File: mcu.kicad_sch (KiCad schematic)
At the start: 1 part, among them U1 STM32F405RGTx

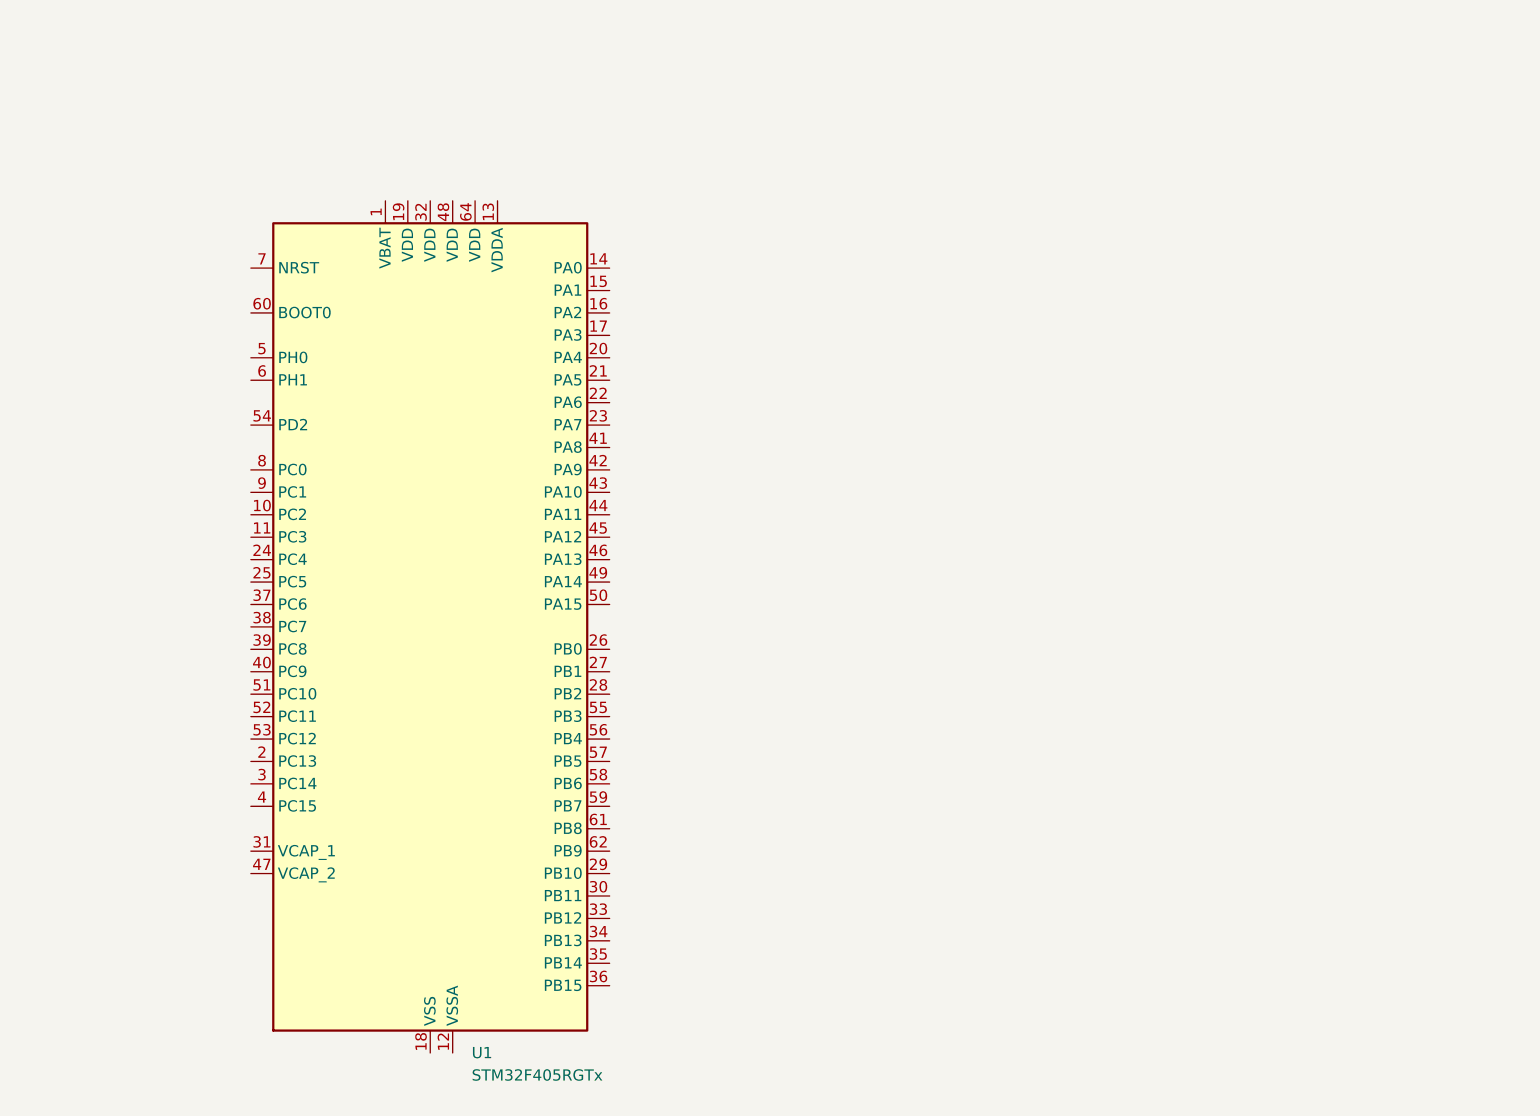
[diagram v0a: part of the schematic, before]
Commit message: Added oled
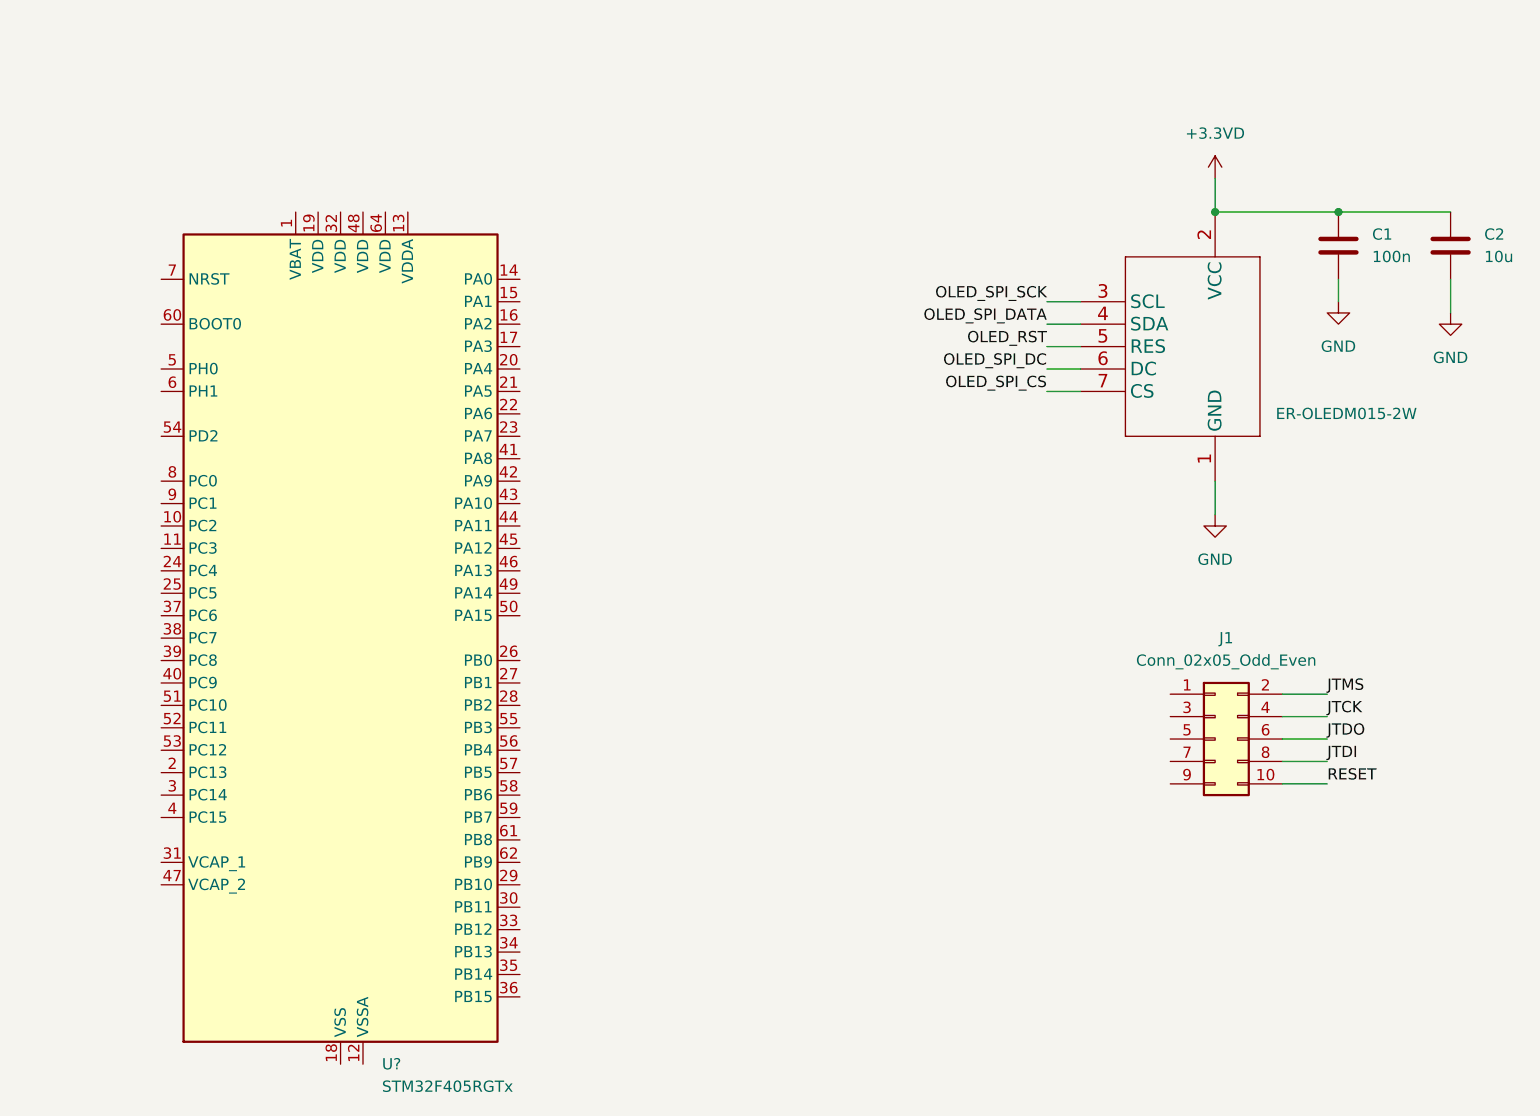
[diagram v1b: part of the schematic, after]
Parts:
- added C1: 100n, symbol Device:C
- added C2: 10u, symbol Device:C
- added ER-OLEDM015-2W: ~, Galerna:ER-OLEDM015-2, symbol Galerna:ER-OLEDM015-SPI
- added J1: Conn_02x05_Odd_Even, symbol Connector_Generic:Conn_02x05_Odd_Even
- renumbered U1 to U?
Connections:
- new net +3.3VD: C1.1, C2.1, ER-OLEDM015-2W.2 (VCC)
- new net GND: C1.2, C2.2, ER-OLEDM015-2W.1 (GND)
- new net JTCK: J1.4 (Pin_4)
- new net JTDI: J1.8 (Pin_8)
- new net JTDO: J1.6 (Pin_6)
- new net JTMS: J1.2 (Pin_2)
- new net OLED_RST: ER-OLEDM015-2W.5 (RES)
- new net OLED_SPI_CS: ER-OLEDM015-2W.7 (CS)
- new net OLED_SPI_DATA: ER-OLEDM015-2W.4 (SDA)
- new net OLED_SPI_DC: ER-OLEDM015-2W.6 (DC)
- new net OLED_SPI_SCK: ER-OLEDM015-2W.3 (SCL)
- new net RESET: J1.10 (Pin_10)
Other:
- moved on the sheet: U?

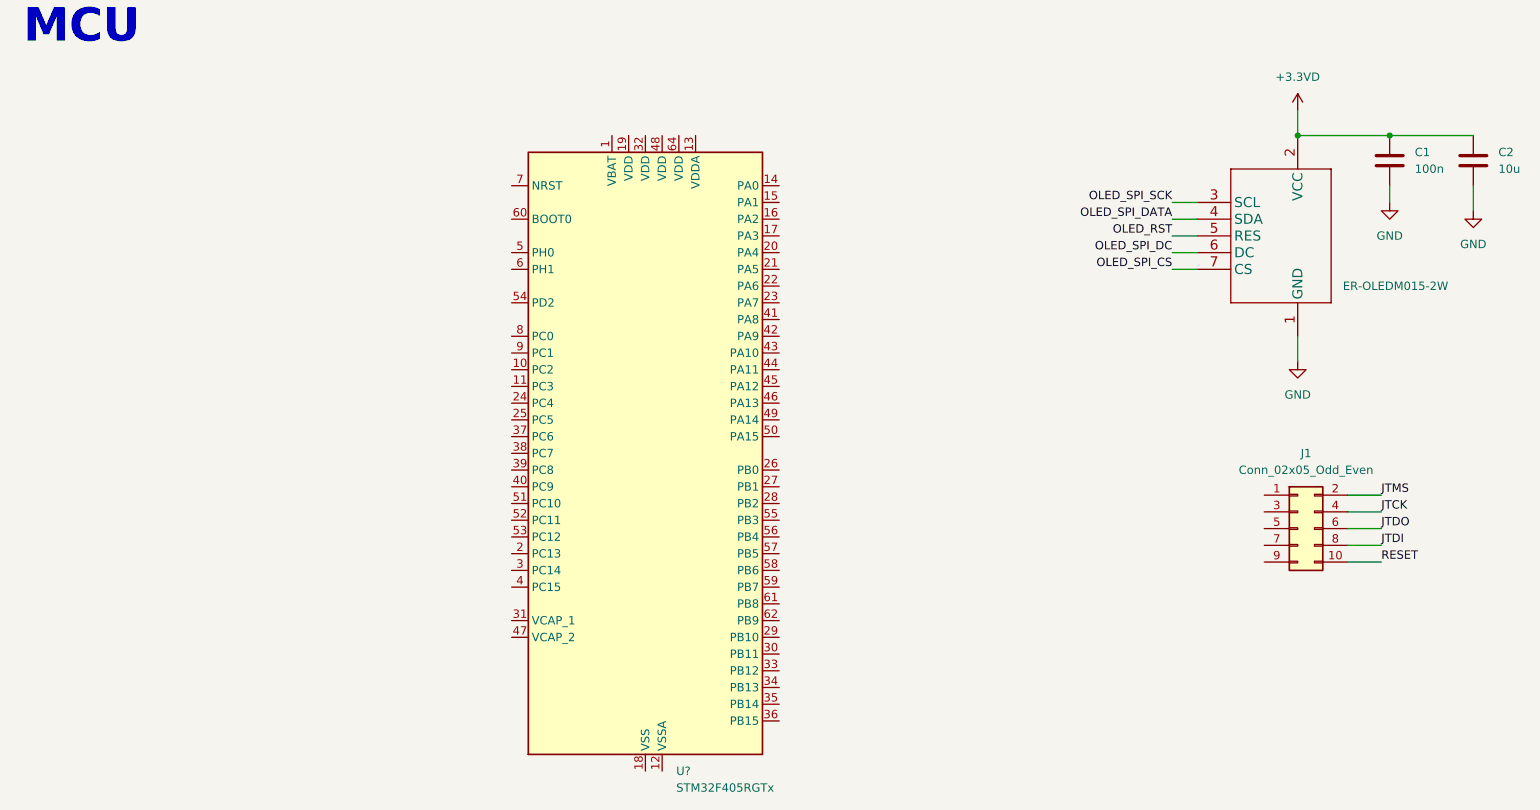
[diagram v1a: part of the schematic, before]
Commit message: SWD connector added
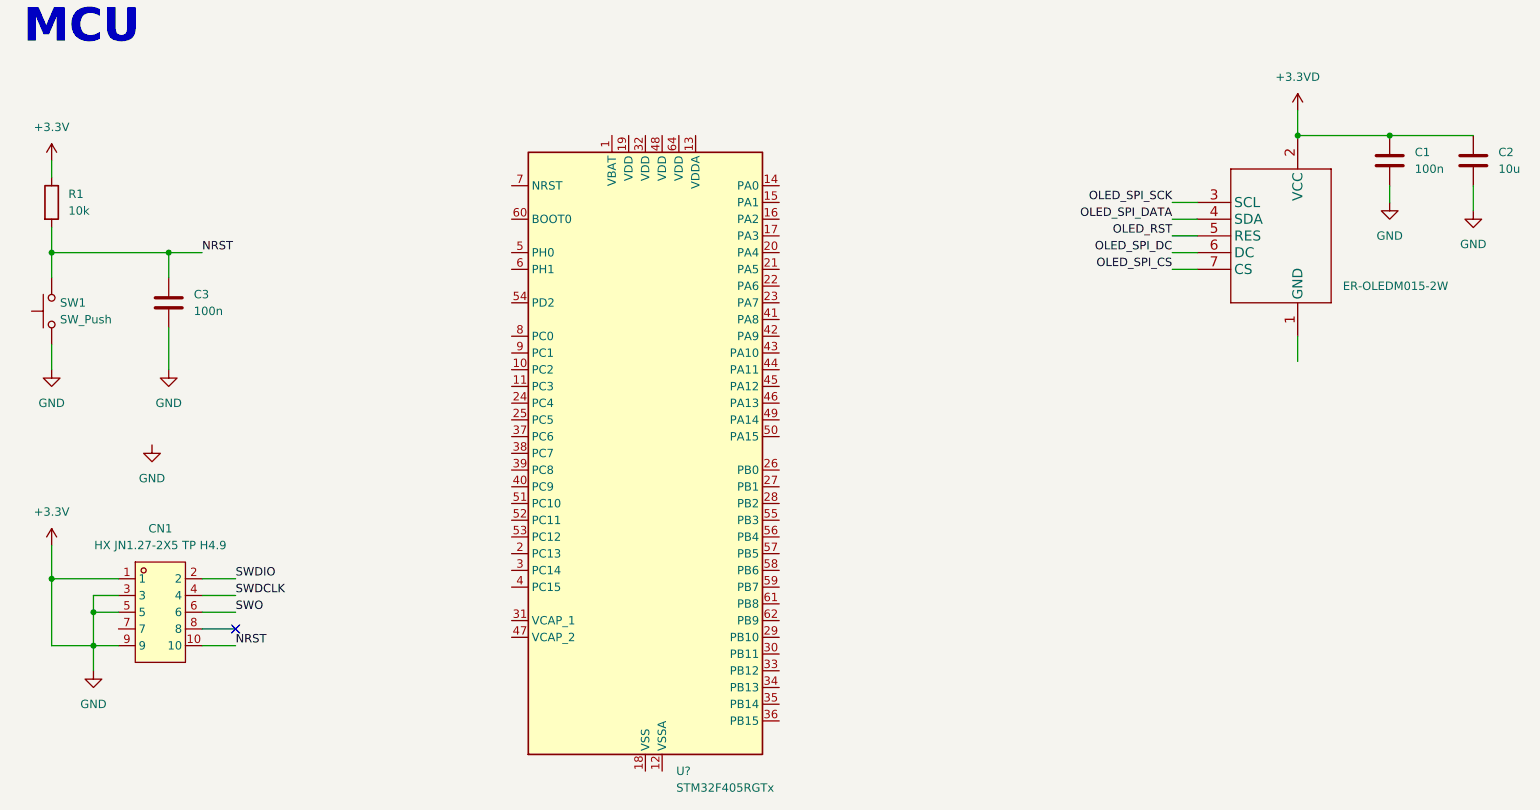
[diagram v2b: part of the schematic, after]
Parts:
- removed J1: Conn_02x05_Odd_Even, symbol Connector_Generic:Conn_02x05_Odd_Even
- added C3: 100n, symbol Device:C
- added CN1: HX JN1.27-2X5 TP H4.9, Galerna:IDC-SMD_10P-P1.27-3220-10-0300-00, symbol Galerna:HXJN1.27-2X5TPH4.9
- added R1: 10k, symbol Device:R
- added SW1: SW_Push, symbol Switch:SW_Push
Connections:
- net GND renamed +3.3V
- net +3.3V: now also C3.2, CN1.1, CN1.3, CN1.5, CN1.9, R1.1, SW1.1; no longer ER-OLEDM015-2W.1 (GND)
- new net NRST: C3.1, CN1.10, R1.2, SW1.2
- new net SWDCLK: CN1.4
- new net SWDIO: CN1.2
- new net SWO: CN1.6
- no-connect marks 0 -> 1

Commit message: extending library
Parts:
- removed SW1: SW_Push, symbol Switch:SW_Push
- added SW1: TS-1088-AR02016, Galerna:SW-SMD_L3.9-W3.0-P4.45, symbol Galerna:TS-1088-AR02016
- gave numbers to parts that had none: 1
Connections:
- net +3.3V: now also SW1.2
- net NRST: now also SW1.1
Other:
- moved on the sheet: C3, CN1, R1

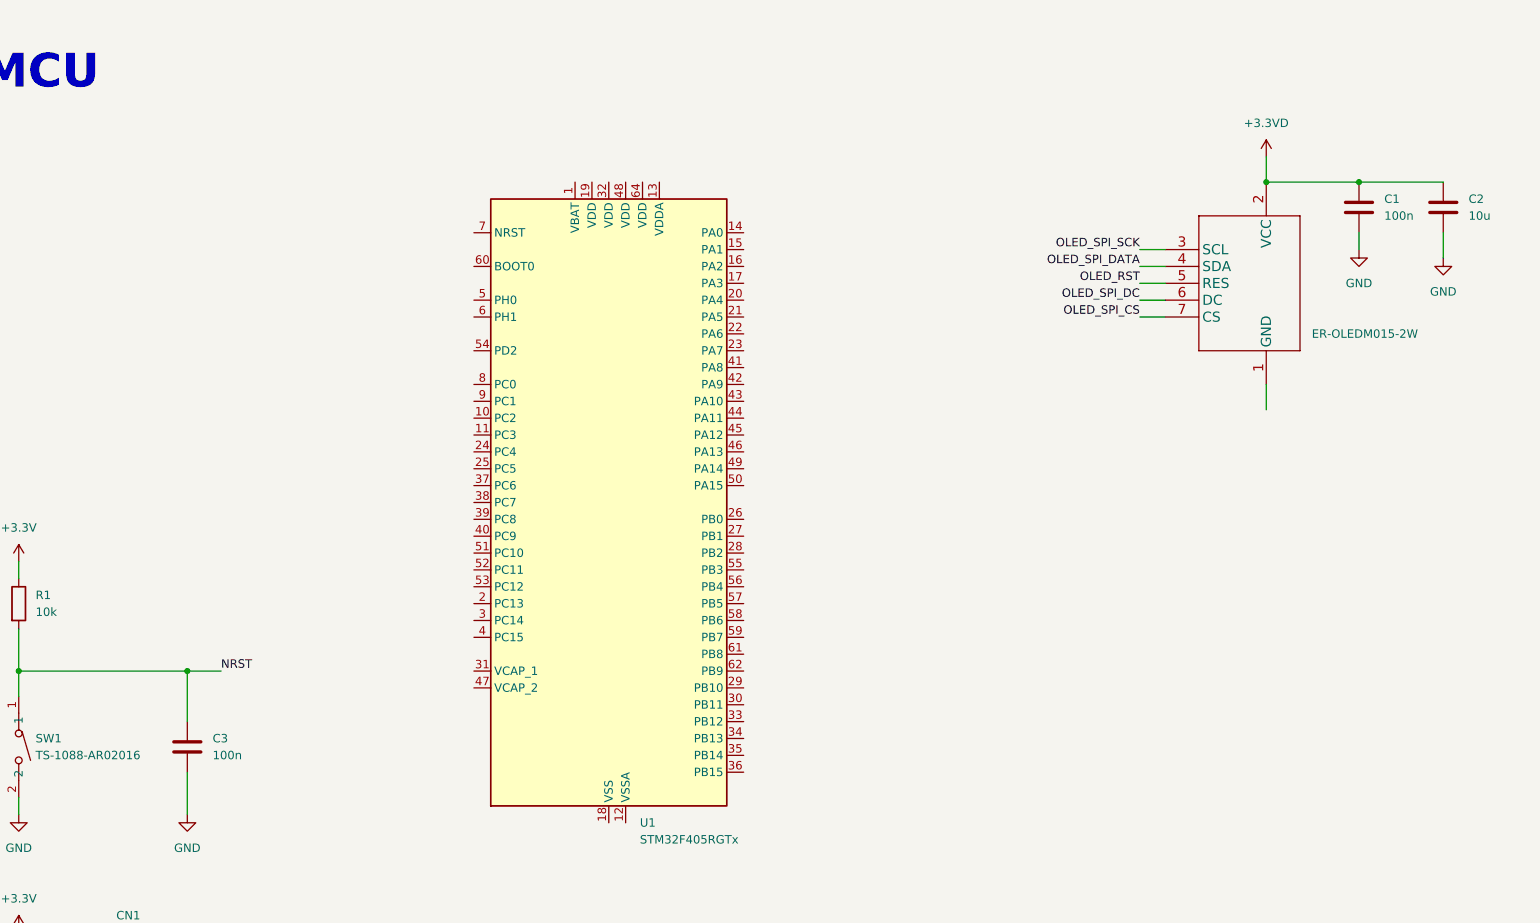
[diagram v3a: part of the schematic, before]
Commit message: adde boot switch
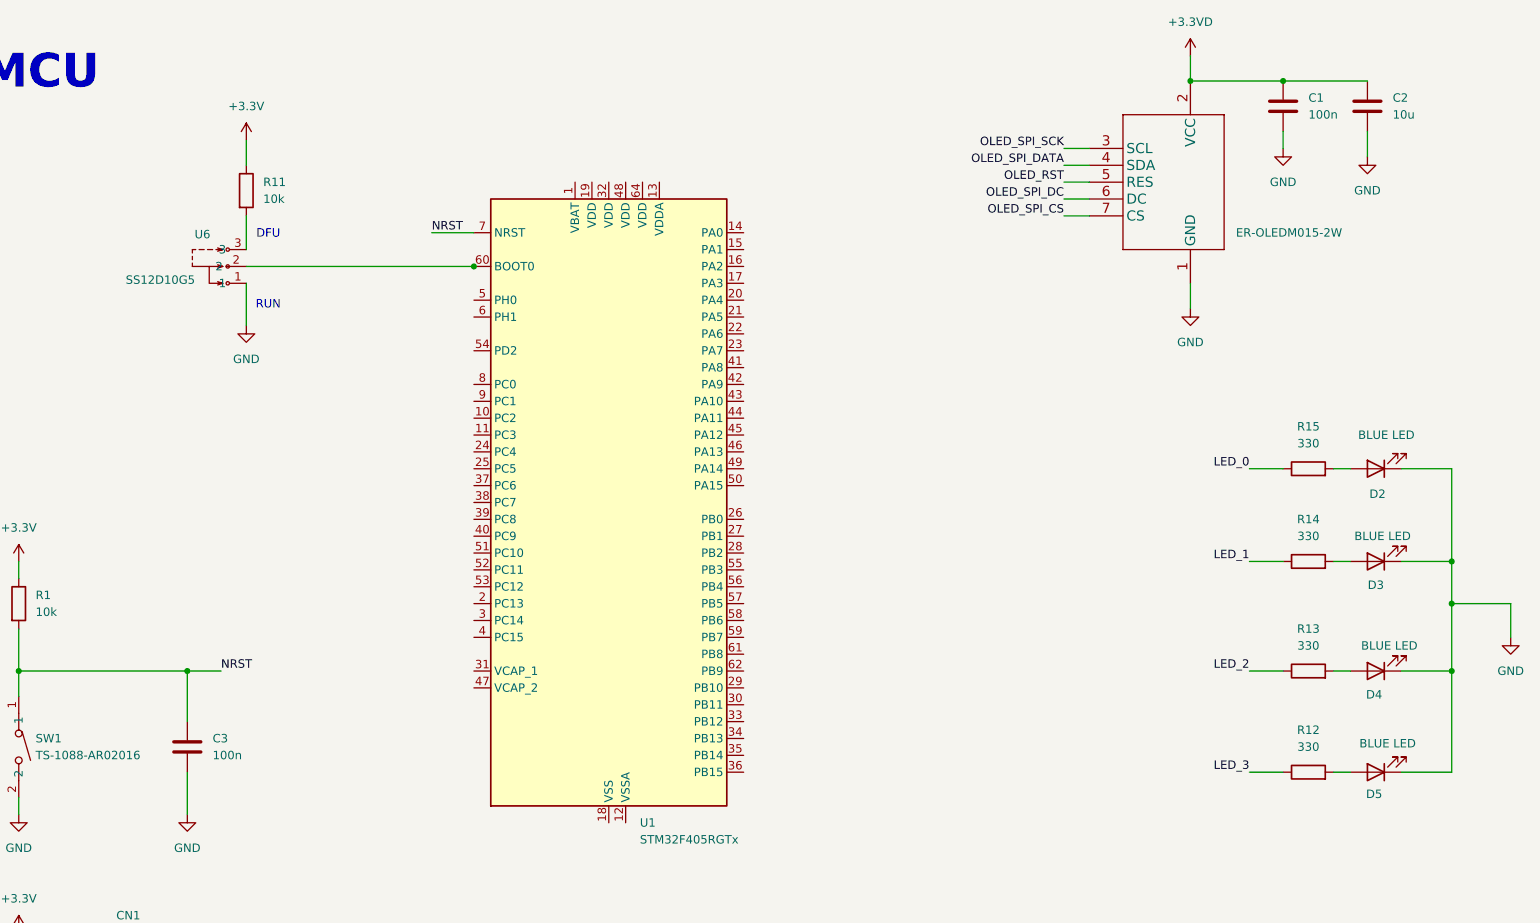
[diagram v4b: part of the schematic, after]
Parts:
- added D2, D3, D4, D5: BLUE LED, symbol Device:LED
- added R11: 10k, symbol Device:R
- added R12, R13, R14, R15: 330, symbol Device:R
- added U6: SS12D10G5, Galerna:SW-TH_SHOU-HAN_SS12D10G4, symbol Galerna:SS12D10G5
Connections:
- net +3.3V: now also ER-OLEDM015-2W.1 (GND), D2.1 (K), D3.1 (K), D4.1 (K), D5.1 (K), R11.1, U6.1
- net NRST: now also U1.7 (NRST)
- net at U1.60 (BOOT0): now also U6.2
- new net: D5.2 (A), R12.2
- new net: D3.2 (A), R14.2
- new net: R11.2, U6.3
- new net: D2.2 (A), R15.2
- new net: D4.2 (A), R13.2
- new net LED_0: R15.1
- new net LED_1: R14.1
- new net LED_2: R13.1
- new net LED_3: R12.1
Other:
- note added: "DFU"
- note added: "RUN"
- moved on the sheet: C1, C2, ER-OLEDM015-2W

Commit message: First pins assingments
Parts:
- removed R11: 10k, symbol Device:R
- added C4: 100n, symbol Device:C
- added C5, C6: 10u, symbol Device:C
- added C7, C8: 12p, symbol Device:C
- added D1: RED, symbol Device:LED
- added FB1: 100@100MHz, symbol Device:FerriteBead
- added J1: DM3CS-SF, Galerna:HRS_DM3CS-SF, symbol Galerna:DM3CS-SF
- added R10: 47k, symbol Device:R
- added R2, R3, R4, R5, R6: 10k, symbol Device:R
- added R7: 22, symbol Device:R
- added R8: 1K, symbol Device:R
- added R9: 10K, symbol Device:R
- added X1: X1E000210127000G, Galerna:CRYSTAL-SMD_4P-L3.2-W2.5-BL, symbol Galerna:X1E000210127000G
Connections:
- net +3.3VD is gone; now on net +3V3: C1.1, C2.1, ER-OLEDM015-2W.2 (VCC)
- net OLED_SPI_DC is gone; now on net OLED_DC: ER-OLEDM015-2W.6 (DC)
- net +3.3V: now also C4.2, C5.2, C6.2, C7.2, C8.2, J1.6 (VSS), J1.S1 (GND), J1.S2 (GND), J1.S3 (GND), J1.S5 (GND), R8.2, X1.2 (GND), X1.4 (GND); no longer R1.1
- net NRST: no longer C3.1, R1.2, SW1.1, U1.7 (NRST)
- net OLED_RST: now also U1.24 (PC4)
- net OLED_SPI_CS: now also U1.20 (PA4)
- net OLED_SPI_DATA: now also U1.23 (PA7)
- net OLED_SPI_SCK: now also U1.21 (PA5)
- net at U6.2: now also D1.2 (A), R9.1; no longer U1.60 (BOOT0)
- net +3V3: now reaches U6.3
- net +3V3: now also R1.1, C6.1, FB1.1, R2.1, R3.1, R4.1, R5.1, R6.1
- net I2S_SDI: now reaches U1.10 (PC2)
- net I2S_SD: now reaches U1.11 (PC3)
- net OLED_DC: now reaches U1.22 (PA6)
- net I2S_CK: now reaches U1.29 (PB10)
- net I2S_WS: now reaches U1.33 (PB12)
- net I2S_MCK: now reaches U1.37 (PC6)
- net HSE_IN: now reaches U1.5 (PH0)
- net HSE_IN: now also C7.1, X1.1 (OSC1)
- net I2S_SCL: now reaches U1.58 (PB6)
- net I2S_SCA: now reaches U1.59 (PB7)
- net HSE_OUT: now reaches U1.6 (PH1)
- net HSE_OUT: now also R10.2
- new net: C8.1, R10.1, X1.3 (OSC2)
- new net: D1.1 (K), R8.1
- new net: J1.5 (CLK), R7.2
- new net +3V3_SD: C4.1, C5.1, FB1.2, J1.4 (VDD)
- new net MCU_BOOT0: R9.2, U1.60 (BOOT0)
- new net MCU_NRST: C3.1, R1.2, SW1.1, U1.7 (NRST)
- new net MCU_SDIO_CK: R7.1
- new net MCU_SDIO_CMD: J1.3 (CMD), R2.2
- new net MCU_SDIO_D0: J1.7 (DAT0), R3.2
- new net MCU_SDIO_D1: J1.8 (DAT1), R4.2
- new net MCU_SDIO_D2: J1.1 (DAT2), R5.2
- new net MCU_SDIO_D3: J1.2 (CD/DAT3), R6.2
- new net SD_CARD_DETECT: J1.9 (CD_SW)
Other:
- moved on the sheet: C1, C2, C3, CN1, D2, D3, D4, D5, ER-OLEDM015-2W, R1, R12, R13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
